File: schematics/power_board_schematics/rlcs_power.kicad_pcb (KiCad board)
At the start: 2 copper layers, 45 x 75 mm, 50 parts, among them J1 SD_Card, J2 Battery Conn, J3 CONN_01X02, J4 CONN_01X02, J5 CONN_01X02, J6 CONN_01X02, J7 CONN_01X16, Q4 Q_NPN_BEC, Q5 Q_NPN_BEC, T1 12 to 3v3, T2 12 to 5, T3 12-15v

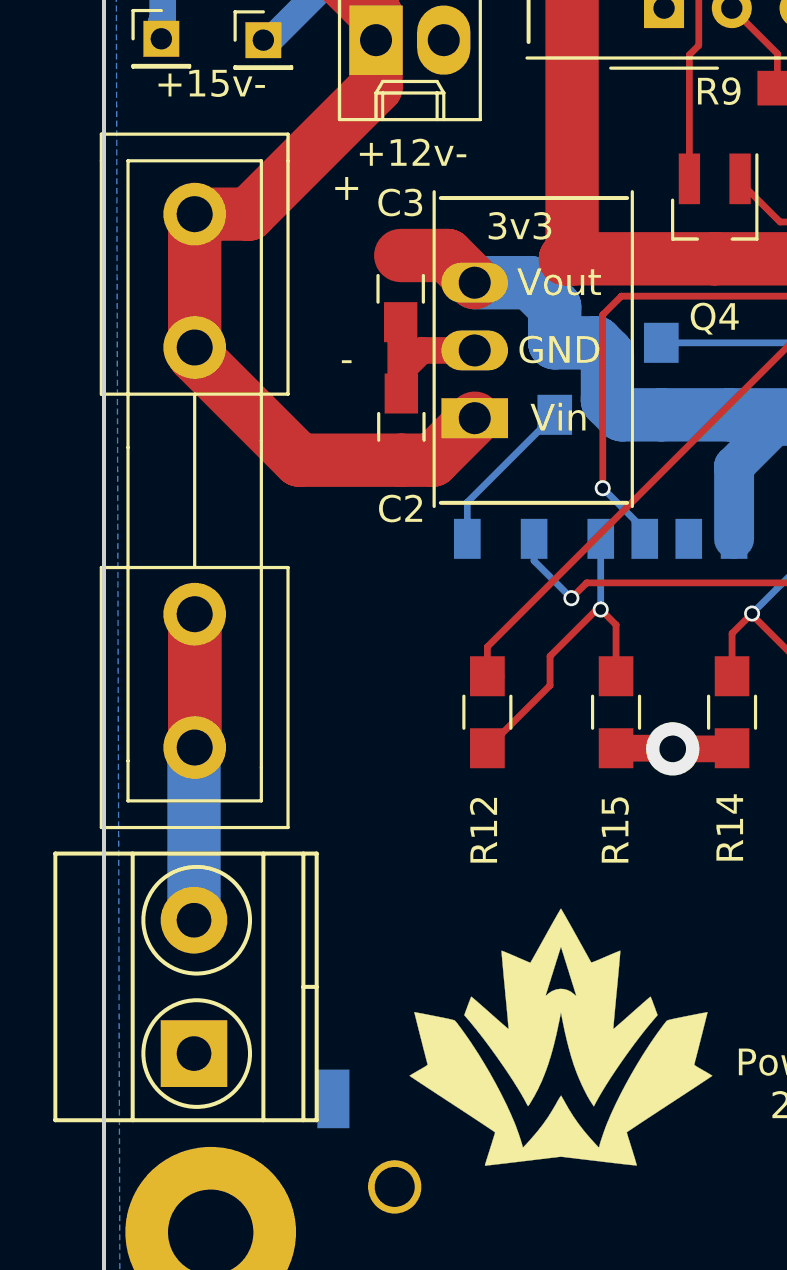
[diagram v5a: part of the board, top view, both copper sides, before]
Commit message: Silkscreen fix on power board
Battery terminal label wasn't where it should have been. It now is
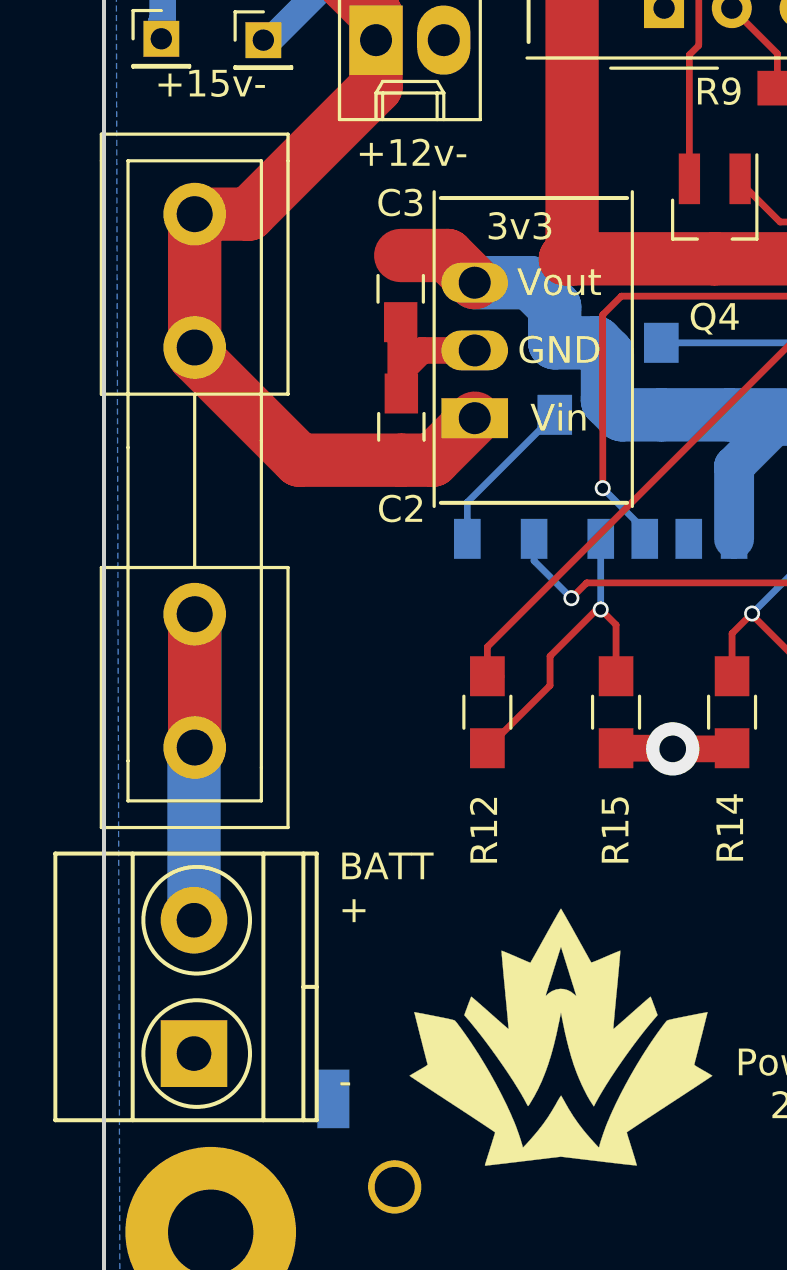
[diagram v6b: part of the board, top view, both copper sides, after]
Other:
- board text added: "BATT + -"
- board text removed: "+ -"
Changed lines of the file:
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@@
   (page A4)
   (layers
-    (0 F.Cu signal)
-    (31 B.Cu signal)
+    (0 F.Cu signal hide)
+    (31 B.Cu signal hide)
     (32 B.Adhes user hide)
     (33 F.Adhes user hide)
@@
     (visible_elements FFFFFFA9)
     (pcbplotparams
-      (layerselection 0x010e0_80000001)
+      (layerselection 0x00020_00000000)
       (usegerberextensions false)
       (excludeedgelayer true)
@@
     (effects (font (size 1 1) (thickness 0.15)))
   )
-  (gr_text "+\n\n\n\n-" (at 109.1 109.05) (layer F.SilkS)
-    (effects (font (size 1 1) (thickness 0.15)))
+  (gr_text "BATT\n+\n\n\n\n-" (at 108.8 135.325) (layer F.SilkS)
+    (effects (font (size 1 1) (thickness 0.15)) (justify left))
   )
   (gr_text +5v- (at 132.35 83.3) (layer F.SilkS)

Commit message: Made the pcb
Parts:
- removed C5: 22uF, Capacitors_SMD:C_0805_HandSoldering
- removed C6: 2.2uF, Capacitors_SMD:C_0805_HandSoldering
- removed G***: LOGO, rlcs_power:rocketry_logo_small_noletters
- removed Q4, Q5: Q_NPN_BEC, TO_SOT_Packages_SMD:SOT-23_Handsoldering
- removed R24: 20K, Resistors_SMD:R_0805_HandSoldering
- removed R26, R27: 10K, Resistors_SMD:R_0805_HandSoldering
- removed REF** (x4): MountingHole_3.2mm_M3_Pad, Mounting_Holes:MountingHole_3.2mm_M3_Pad
- removed T3: 12-15v, rlcs_power:VEFT1-S-SMD
- removed TP0: GND_test, Socket_Strips:Socket_Strip_Straight_1x01_Pitch2.00mm
- removed TP5: 15v-, Socket_Strips:Socket_Strip_Straight_1x01_Pitch2.00mm
- added C4: 22uF, Capacitor_SMD:C_0805_2012Metric_Pad1.15x1.40mm_HandSolder, B.Cu at (137.2, 74.9)
- added J10: Conn_14_to_21, Connector_PinSocket_2.54mm:PinSocket_1x08_P2.54mm_Vertical, F.Cu at (146.1, 135.9)
- added J11: conn_power, Connector_PinSocket_2.54mm:PinSocket_1x08_P2.54mm_Vertical, F.Cu at (95.2, 95.2)
- added J12: conn_A8_to_A15, Connector_PinSocket_2.54mm:PinSocket_1x08_P2.54mm_Vertical, F.Cu at (95.2, 141.0)
- added J13: conn_A0_to_A7, Connector_PinSocket_2.54mm:PinSocket_1x08_P2.54mm_Vertical, F.Cu at (95.2, 118.1)
- added J14: conn_22_to_53, Connector_PinSocket_2.54mm:PinSocket_2x18_P2.54mm_Vertical, F.Cu at (102.9, 161.3)
- added J8: Conn_0_to_7, Connector_PinSocket_2.54mm:PinSocket_1x08_P2.54mm_Vertical, F.Cu at (146.1, 113.0)
- added J9: conn_8_to_13, Connector_PinHeader_2.54mm:PinHeader_1x10_P2.54mm_Vertical, F.Cu at (146.1, 85.1)
- added Q1: Q_NPN_BEC, Package_TO_SOT_SMD:SOT-23-5_HandSoldering, F.Cu at (124.5, 80.0)
- added Q1: Q_NPN_BEC, Package_TO_SOT_SMD:SOT-23-5_HandSoldering, F.Cu at (119.4, 80.0)
- added Q2: Q_NPN_BEC, Package_TO_SOT_SMD:SOT-23-5_HandSoldering, F.Cu at (124.5, 97.8)
- added Q2: Q_NPN_BEC, Package_TO_SOT_SMD:SOT-23-5_HandSoldering, F.Cu at (115.6, 97.8)
- added R1: 20K, Resistor_SMD:R_0805_2012Metric_Pad1.15x1.40mm_HandSolder, F.Cu at (114.3, 138.3)
- added R16: 20K, Resistor_SMD:R_0805_2012Metric_Pad1.15x1.40mm_HandSolder, F.Cu at (120.7, 113.0)
- added R17: 10K, Resistor_SMD:R_0805_2012Metric_Pad1.15x1.40mm_HandSolder, F.Cu at (137.2, 99.1)
- added R17: 10K, Resistor_SMD:R_0805_2012Metric_Pad1.15x1.40mm_HandSolder, F.Cu at (133.1, 100.4)
- added R18: 10K, Resistor_SMD:R_0805_2012Metric_Pad1.15x1.40mm_HandSolder, F.Cu at (139.7, 99.1)
- added R18: 10K, Resistor_SMD:R_0805_2012Metric_Pad1.15x1.40mm_HandSolder, F.Cu at (133.3, 104.1)
- added S1: SW_Push, Button_Switch_SMD:SW_DIP_SPSTx01_Slide_9.78x4.72mm_W8.61mm_P2.54mm, F.Cu at (96.5, 82.5)
- added TP3: GND_test, Connector_PinSocket_2.00mm:PinSocket_1x01_P2.00mm_Vertical, F.Cu at (128.3, 87.6)
- C1: footprint Capacitors_SMD:C_0805_HandSoldering -> Capacitor_SMD:C_0805_2012Metric_Pad1.15x1.40mm_HandSolder
- C2: value 10uF -> 22uF; footprint Capacitors_SMD:C_0805_HandSoldering -> Capacitor_SMD:C_0805_2012Metric_Pad1.15x1.40mm_HandSolder
- C3: value 22uF -> 10uF; footprint Capacitors_SMD:C_0805_HandSoldering -> Capacitor_SMD:C_0805_2012Metric_Pad1.15x1.40mm_HandSolder
- C4: value 1uF -> 22uF; footprint Capacitors_SMD:C_0805_HandSoldering -> Capacitor_SMD:C_0805_2012Metric_Pad1.15x1.40mm_HandSolder
- J1: footprint rlcs_power:SDCARD -> rlcs_power_footprints:SDCARD
- J2: value Battery Conn -> Conn_01x05_Male; footprint Connectors_Terminal_Blocks:TerminalBlock_Pheonix_MKDS1.5-2pol -> Connector_JST:JST_EH_B5B-EH-A_1x05_P2.50mm_Vertical
- J3: value CONN_01X02 -> Conn_01x05_Male; footprint Connectors_Molex:Molex_KK-6410-02_02x2.54mm_Straight -> Connector_JST:JST_EH_B5B-EH-A_1x05_P2.50mm_Vertical
- J4: value CONN_01X02 -> Battery Conn; footprint Connectors_Molex:Molex_KK-6410-02_02x2.54mm_Straight -> TerminalBlock_Phoenix:TerminalBlock_Phoenix_MKDS-1,5-2_1x02_P5.00mm_Horizontal
- J5, J6: footprint Connectors_Molex:Molex_KK-6410-02_02x2.54mm_Straight -> Connector_Molex:Molex_KK-254_AE-6410-02A_1x02_P2.54mm_Vertical
- J7: value CONN_01X16 -> CONN_01X02; footprint Pin_Headers:Pin_Header_Straight_2x08_Pitch2.54mm -> Connector_Molex:Molex_KK-254_AE-6410-02A_1x02_P2.54mm_Vertical
- JP1: footprint Pin_Headers:Pin_Header_Straight_1x03_Pitch2.54mm -> Connector_PinHeader_2.54mm:PinHeader_1x03_P2.54mm_Horizontal
- R1: value 10K -> 20K; footprint Resistors_SMD:R_0805_HandSoldering -> Resistor_SMD:R_0805_2012Metric_Pad1.15x1.40mm_HandSolder
- R10, R11, R14: value 20K -> 150; footprint Resistors_SMD:R_0805_HandSoldering -> Resistor_SMD:R_0805_2012Metric_Pad1.15x1.40mm_HandSolder
- R12, R13: value 10K -> 150; footprint Resistors_SMD:R_0805_HandSoldering -> Resistor_SMD:R_0805_2012Metric_Pad1.15x1.40mm_HandSolder
- R15, R7, R8, R9: footprint Resistors_SMD:R_0805_HandSoldering -> Resistor_SMD:R_0805_2012Metric_Pad1.15x1.40mm_HandSolder
- R2, R3, R4: value 150 -> 10K; footprint Resistors_SMD:R_0805_HandSoldering -> Resistor_SMD:R_0805_2012Metric_Pad1.15x1.40mm_HandSolder
- R5: value 150 -> 20K; footprint Resistors_SMD:R_0805_HandSoldering -> Resistor_SMD:R_0805_2012Metric_Pad1.15x1.40mm_HandSolder; moved to F.Cu
- R6: value 150 -> 20K; footprint Resistors_SMD:R_0805_HandSoldering -> Resistor_SMD:R_0805_2012Metric_Pad1.15x1.40mm_HandSolder
- T1, T2: footprint rlcs_power:VXO78XX-1000 -> rlcs_power_footprints:VXO78XX-1000
- TP1: value 5v_test -> 12v_test; footprint Socket_Strips:Socket_Strip_Straight_1x01_Pitch2.00mm -> Connector_PinSocket_2.00mm:PinSocket_1x01_P2.00mm_Vertical
- TP2: footprint Socket_Strips:Socket_Strip_Straight_1x01_Pitch2.00mm -> Connector_PinSocket_2.00mm:PinSocket_1x01_P2.00mm_Vertical
- TP3: value 12v_test -> GND_test; footprint Socket_Strips:Socket_Strip_Straight_1x01_Pitch2.00mm -> Connector_PinSocket_2.00mm:PinSocket_1x01_P2.00mm_Vertical
- TP4: value 15v+ -> 5v_test; footprint Socket_Strips:Socket_Strip_Straight_1x01_Pitch2.00mm -> Connector_PinSocket_2.00mm:PinSocket_1x01_P2.00mm_Vertical
- moved J4 64.9 mm to (108.0, 139.7), turned to 180 degrees
- moved R2 53.5 mm to (119.4, 138.4), turned to 270 degrees
- moved R13 38.6 mm to (116.8, 88.7)
- moved R14 38.0 mm to (114.3, 88.7)
- moved R12 37.2 mm to (119.4, 88.7)
- moved R11 36.6 mm to (137.2, 82.5), turned to 90 degrees
- moved R10 35.8 mm to (139.7, 82.5)
- moved R1 29.8 mm to (116.8, 138.4)
- moved C3 28.9 mm to (105.4, 81.3), turned to 0 degrees
- moved TP1 28.4 mm to (114.3, 71.1)
- moved JP1 25.6 mm to (118.1, 130.8)
- moved J7 25.4 mm to (125.7, 128.3)
- moved J2 24.9 mm to (127.0, 146.1), turned to 0 degrees
- moved R6 21.2 mm to (137.2, 78.7), turned to 90 degrees
- moved R7 20.5 mm to (139.7, 74.9), turned to 90 degrees
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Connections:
- C1 pad 1: +12P -> +12V
- C2 pad 1: +12P -> +3V3
- C3 pad 1: +3V3 -> +12V
- C4 pad 1: +12P -> +5V
- F1 pad 2: +12P -> +12V
- J2 pad 1: GND -> /SDA
- J2 pad 2: Net-(F1-Pad1) -> /SCL
- J3 pad 1: +3V3 -> /SDA
- J3 pad 2: GND -> /SCL
- J4 pad 1: +5V -> GND
- J4 pad 2: GND -> Net-(F1-Pad1)
- J5 pad 1: +15V -> +12V
- J5 pad 2: GNDREF -> GND
- J6 pad 1: +12P -> +5V
- J7 pad 1: ARD_CON_SD_SS -> +3V3
- J7 pad 2: ARD_CON_SD_MISO -> GND
- R1 pad 1: GND -> Net-(JP1-Pad1)
- R1 pad 2: Net-(JP1-Pad1) -> ARD_CON_SD_SS
- R10 pad 1: +3V3 -> Sevenseg_D
- R10 pad 2: Net-(J1-Pad8) -> Net-(AFF1-Pad5)
- R11 pad 1: +3V3 -> Sevenseg_C
- R11 pad 2: Net-(J1-Pad9) -> Net-(AFF1-Pad1)
- R12 pad 1: Net-(J1-Pad2) -> Sevenseg_B
- R12 pad 2: ARD_CON_SD_MOSI -> Net-(AFF1-Pad8)
- R13 pad 1: Net-(J1-Pad5) -> Sevenseg_A
- R13 pad 2: ARD_CON_SD_SCL -> Net-(AFF1-Pad10)
- R14 pad 1: Net-(J1-Pad5) -> Sevenseg_DP
- R14 pad 2: GND -> Net-(AFF1-Pad2)
- R15 pad 1: Net-(J1-Pad2) -> +3V3
- R15 pad 2: GND -> Net-(J1-Pad8)
- R2 pad 1: ARD_CON_7SEG_G -> GND
- R2 pad 2: Net-(AFF1-Pad7) -> Net-(JP1-Pad1)
- R3 pad 1: ARD_CON_7SEG_F -> Net-(J1-Pad2)
- R3 pad 2: Net-(AFF1-Pad6) -> ARD_CON_SD_MOSI
- R4 pad 1: ARD_CON_7SEG_E -> Net-(J1-Pad5)
- R4 pad 2: Net-(AFF1-Pad3) -> ARD_CON_SD_SCL
- R5 pad 1: ARD_CON_7SEG_D -> Net-(J1-Pad5)
- R5 pad 2: Net-(AFF1-Pad5) -> GND
- R6 pad 1: ARD_CON_7SEG_C -> Net-(J1-Pad2)
- R6 pad 2: Net-(AFF1-Pad1) -> GND
- R7 pad 1: ARD_CON_7SEG_B -> Sevenseg_G
- R7 pad 2: Net-(AFF1-Pad8) -> Net-(AFF1-Pad7)
- R8 pad 1: ARD_CON_7SEG_A -> Sevenseg_F
- R8 pad 2: Net-(AFF1-Pad10) -> Net-(AFF1-Pad6)
- R9 pad 1: ARD_CON_7SEG_DP -> Sevenseg_E
- R9 pad 2: Net-(AFF1-Pad2) -> Net-(AFF1-Pad3)
- T1 pad 1: +12P -> +12V
- T2 pad 1: +12P -> +12V
- TP1 pad 1: +5V -> +12V
- TP3 pad 1: +12P -> GND
- TP4 pad 1: +15V -> +5V
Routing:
- net +12P: track 74.5 -> 0.00 mm
- net +5V: track 74.1 -> 0.00 mm
- net +3V3: track 54.5 -> 0.00 mm, vias 1 -> 0
- net ARD_CON_SD_CD: track 40.3 -> 0.00 mm, vias 1 -> 0
- net ARD_CON_SD_MOSI: track 38.1 -> 0.00 mm
- net GNDREF: track 32.9 -> 0.00 mm, vias 2 -> 0
- net Net-(J1-Pad1): track 29.4 -> 0.00 mm, vias 3 -> 0
- net +15V: track 28.4 -> 0.00 mm, vias 1 -> 0
- net ARD_CON_SD_SCL: track 26.0 -> 0.00 mm, vias 2 -> 0
- net GND: track 25.8 -> 0.00 mm, vias 2 -> 0
- net ARD_CON_7SEG_A: track 24.0 -> 0.00 mm
- net ARD_CON_7SEG_D2: track 22.2 -> 0.00 mm
- net ARD_CON_7SEG_C: track 20.5 -> 0.00 mm, vias 1 -> 0
- net ARD_CON_SD_WP: track 18.8 -> 0.00 mm, vias 1 -> 0
- net ARD_CON_SD_MISO: track 18.2 -> 0.00 mm, vias 1 -> 0
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- removed copper zone on B.Cu, net GND
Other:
- board size 45 x 75 mm -> 124.5 x 101.6 mm
- board text removed: "+"
- board text removed: "+12v-"
- board text removed: "+5v-"
- board text removed: "-"
- board text removed: "0v"
- board text removed: "15v"
- board text removed: "BATT + -"

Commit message: Updated pcb
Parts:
- J9: footprint Connector_PinHeader_2.54mm:PinHeader_1x10_P2.54mm_Vertical -> Connector_PinSocket_2.54mm:PinSocket_1x10_P2.54mm_Vertical
- moved R7 5.68 mm to (142.2, 69.8)
- moved C4 5.68 mm to (139.7, 69.8)
- moved R10 5.68 mm to (142.2, 77.5)
- moved R3 5.68 mm to (142.2, 73.7)
- moved R11 5.68 mm to (139.7, 77.5)
- moved R6 5.68 mm to (139.7, 73.7)
- moved TP3 5.68 mm to (133.3, 90.2)
- moved AFF1 2.54 mm to (115.6, 96.5)
- moved Q2 2.54 mm to (124.5, 100.3)
- moved Q2 2.54 mm to (115.6, 100.3)
- moved R12 2.54 mm to (119.4, 91.2)
- moved R13 2.54 mm to (116.8, 91.2)
- moved R14 2.54 mm to (114.3, 91.2)
- moved R8 2.54 mm to (121.9, 91.4)
- moved R9 2.29 mm to (124.5, 91.2)
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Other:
- board size 124.5 x 101.6 mm -> 53.3 x 101.6 mm
